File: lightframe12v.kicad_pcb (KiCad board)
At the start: 2 copper layers, 91.4 x 45.7 mm, 44 parts, among them J1 PJ-077, J2 Conn_01x06_Female, J3 Conn_01x02_Female, J4 Conn_01x06_Female, J5 Conn_01x04_Female, J6 Conn_01x6_Female, Q1 MMBT2222A-TP, Q2 MMBT2222A-TP, SW1 SW_Push, SW2 SW_Push, U1 TPS562211, U2 ESP32-WROOM-32U, U3 TLC5971

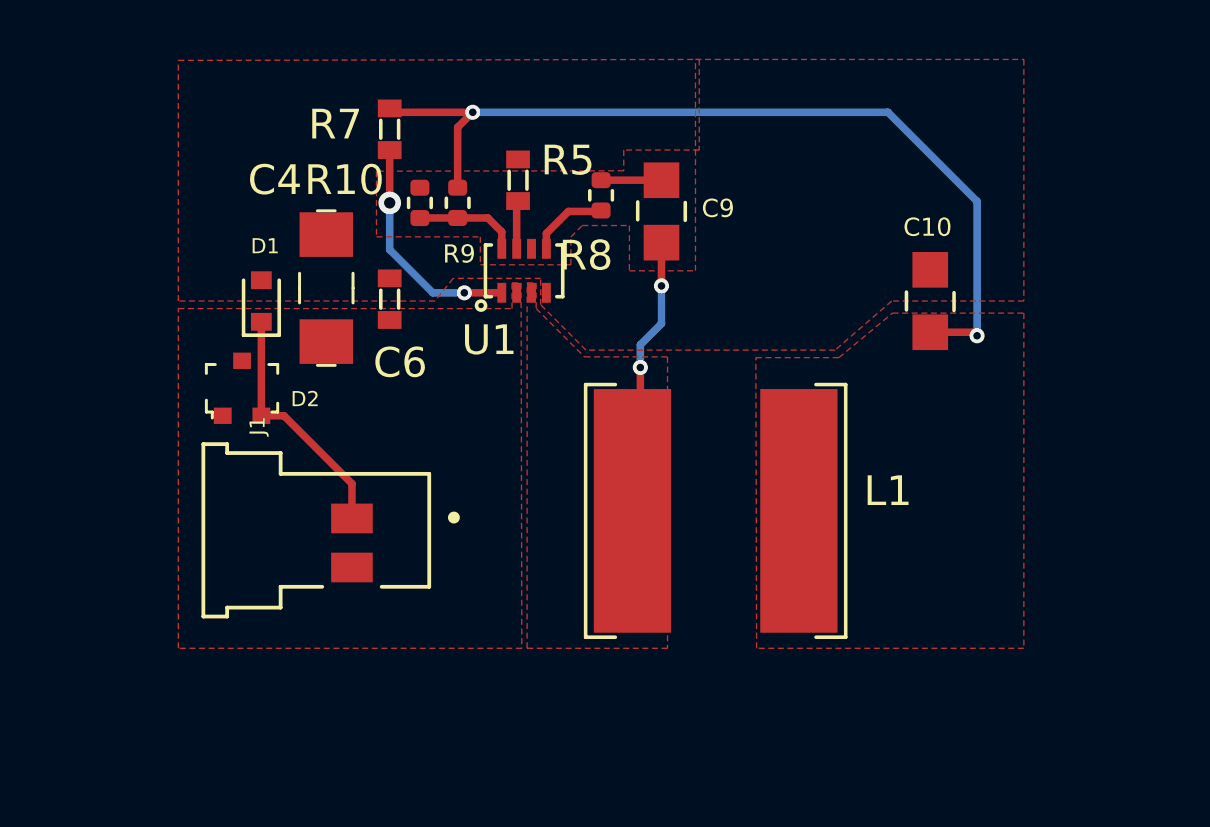
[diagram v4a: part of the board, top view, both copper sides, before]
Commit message: Top ground no cutouts.
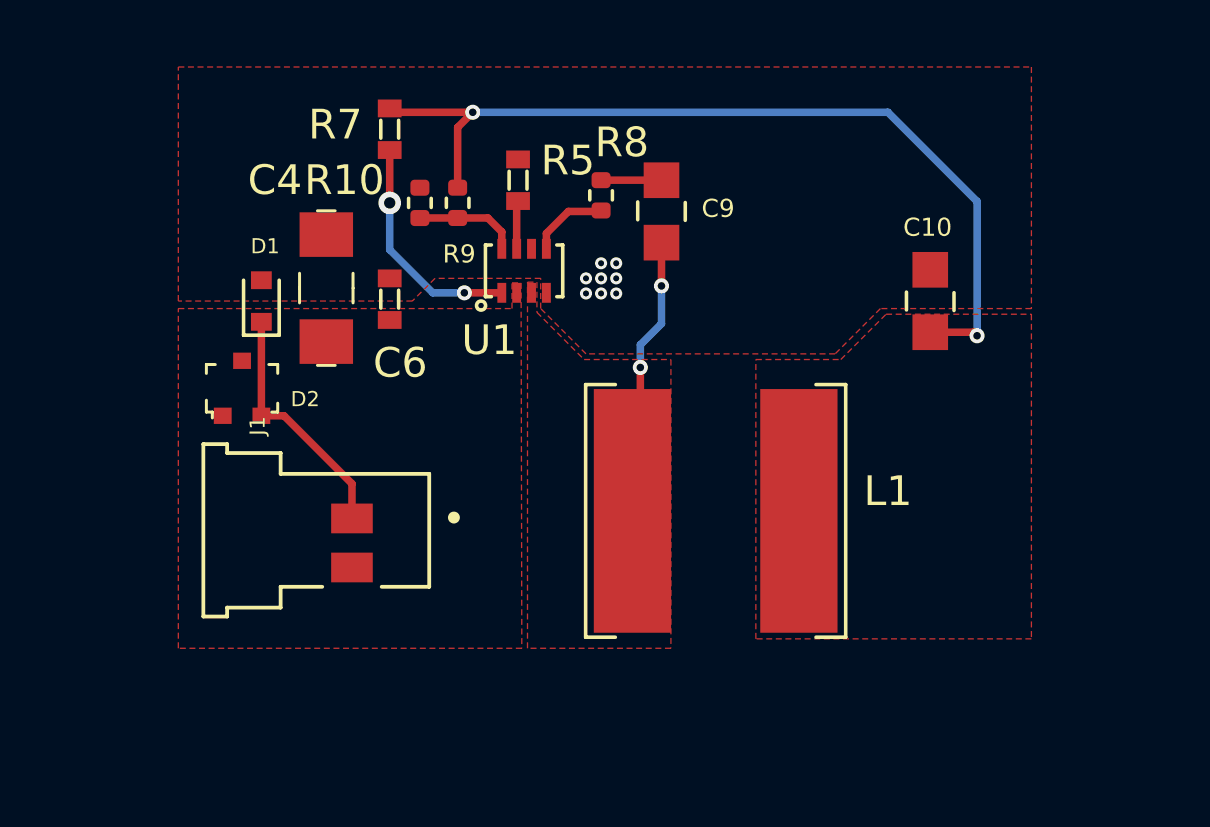
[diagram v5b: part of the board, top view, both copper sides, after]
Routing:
- net GND: vias 18 -> 26
- removed copper zone on F.Cu, net +3V3
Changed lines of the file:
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@@
     (thickness 1.6)
     (drawings 4)
-    (tracks 339)
+    (tracks 347)
     (zones 0)
     (modules 44)
@@
     (tags resistor)
     (attr smd)
-    (fp_text reference R8 (at -2.032 -0.508 180) (layer F.SilkS)
+    (fp_text reference R8 (at 1.778 0.6985 180) (layer F.SilkS)
       (effects (font (size 1 1) (thickness 0.15)))
     )
@@
   (segment (start 280.67 -530.352) (end 280.67 -530.352) (width 0.254) (layer F.Cu) (net 1))
   (via (at 280.67 -530.352) (size 0.508) (drill 0.254) (layers F.Cu B.Cu) (net 1))
+  (via (at 345.44 -560.324) (size 0.4064) (drill 0.2032) (layers F.Cu B.Cu) (net 1))
+  (via (at 345.44 -559.816) (size 0.4064) (drill 0.2032) (layers F.Cu B.Cu) (net 1))
+  (via (at 345.948 -559.816) (size 0.4064) (drill 0.2032) (layers F.Cu B.Cu) (net 1))
+  (via (at 345.948 -560.324) (size 0.4064) (drill 0.2032) (layers F.Cu B.Cu) (net 1))
+  (via (at 346.456 -560.324) (size 0.4064) (drill 0.2032) (layers F.Cu B.Cu) (net 1))
+  (via (at 346.456 -559.816) (size 0.4064) (drill 0.2032) (layers F.Cu B.Cu) (net 1))
+  (via (at 345.948 -560.832) (size 0.4064) (drill 0.2032) (layers F.Cu B.Cu) (net 1))
+  (via (at 346.456 -560.832) (size 0.4064) (drill 0.2032) (layers F.Cu B.Cu) (net 1))
   (segment (start 321.564 -530.606) (end 313.436 -530.606) (width 0.508) (layer F.Cu) (net 2))
   (segment (start 311.402 -532.64) (end 313.436 -530.606) (width 0.508) (layer F.Cu) (net 2))
@@
     )
   )
-  (zone (net 38) (net_name "Net-(C9-Pad2)") (layer F.Cu) (hatch edge 0.508)
+  (zone (net 1) (net_name GND) (layer F.Cu) (hatch full 0.508)
     (connect_pads (clearance 0.1524))
     (min_thickness 0.254)
@@
     (polygon
       (pts
-        (xy 343.7636 -559.308) (xy 345.3892 -557.6824) (xy 348.1832 -557.6824) (xy 348.1832 -547.878) (xy 343.4588 -547.878)
-        (xy 343.4588 -560.1716) (xy 343.7636 -560.1716)
+        (xy 360.426 -559.308) (xy 355.346 -559.308) (xy 353.822 -557.784) (xy 345.44 -557.784) (xy 343.916 -559.308)
+        (xy 343.916 -560.324) (xy 340.36 -560.324) (xy 339.598 -559.562) (xy 331.724 -559.562) (xy 331.724 -567.436)
+        (xy 360.426 -567.436)
       )
     )
   )
-  (zone (net 2) (net_name +3V3) (layer F.Cu) (hatch edge 0.508)
+  (zone (net 38) (net_name "Net-(C9-Pad2)") (layer F.Cu) (hatch full 0.508)
     (connect_pads (clearance 0.1524))
     (min_thickness 0.254)
@@
     (polygon
       (pts
-        (xy 360.172 -547.878) (xy 351.1804 -547.878) (xy 351.155 -557.657) (xy 353.949 -557.657) (xy 355.7524 -559.1556)
-        (xy 360.172 -559.1556)
+        (xy 343.789 -559.181) (xy 345.3765 -557.5935) (xy 348.2975 -557.5935) (xy 348.2975 -547.878) (xy 343.4715 -547.878)
+        (xy 343.4715 -560.197) (xy 343.789 -560.197)
       )
     )
   )
-  (zone (net 1) (net_name GND) (layer F.Cu) (hatch edge 0.508)
+  (zone (net 38) (net_name "Net-(C9-Pad2)") (layer F.Cu) (hatch full 0.508)
     (connect_pads (clearance 0.1524))
     (min_thickness 0.254)
@@
     (polygon
       (pts
-        (xy 349.25 -567.69) (xy 349.25 -564.642) (xy 346.71 -564.642) (xy 346.71 -563.9435) (xy 338.3915 -563.930863)
-        (xy 338.3915 -561.721) (xy 341.884 -561.721) (xy 341.884 -560.7812) (xy 344.932 -560.7812) (xy 344.932 -561.721)
-        (xy 345.313 -562.102) (xy 346.9005 -562.102) (xy 346.9005 -560.578) (xy 349.123 -560.578) (xy 349.123 -567.69)
-        (xy 360.172 -567.69) (xy 360.172 -559.562) (xy 355.727 -559.562) (xy 353.822 -557.911) (xy 345.44 -557.911)
-        (xy 343.916 -559.435) (xy 343.916 -560.324) (xy 340.9696 -560.324) (xy 340.36 -559.562) (xy 331.724 -559.562)
-        (xy 331.724 -567.65825)
+        (xy 360.426 -548.1955) (xy 351.155 -548.1955) (xy 351.155 -557.5935) (xy 354.0125 -557.5935) (xy 355.5365 -559.1175)
+        (xy 360.426 -559.1175)
       )
     )

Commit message: Pmic refactor.
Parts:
- added TP1: wall in, TestPoint:TestPoint_Pad_1.5x1.5mm, F.Cu at (340.9, -550.0)
- added TP3: pgss, TestPoint:TestPoint_Pad_1.5x1.5mm, F.Cu at (332.5, -563.4)
- added TP4: 3v3 out, TestPoint:TestPoint_Pad_1.5x1.5mm, F.Cu at (358.0, -548.6)
- R10, R8, R9: footprint Resistor_SMD:R_0402_1005Metric -> digikey-footprints:0603
- moved R7 3.42 mm to (335.7, -564.1)
- moved J1 2.79 mm to (334.1, -550.0)
- moved C4 2.28 mm to (337.6, -557.9)
- moved C10 2.03 mm to (355.8, -557.9)
- moved D2 1.89 mm to (332.6, -555.2)
- moved R10 1.79 mm to (338.1, -562.7)
- moved C6 1.71 mm to (340.1, -558.5)
- moved D1 1.48 mm to (333.9, -558.2)
- moved U1 1.40 mm to (343.4, -559.2)
- moved L1 1.07 mm to (349.8, -551.4)
- moved R5 0.96 mm to (343.0, -562.7)
- moved C9 0.72 mm to (348.5, -562.1)
- moved R9 0.66 mm to (340.5, -562.7)
- moved R8 0.46 mm to (345.8, -562.7)
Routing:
- net Net-(R7-Pad2): track 7.73 -> 14.6 mm
- net Net-(R10-Pad1): track 3.52 -> 5.87 mm
- net +3V3: track 86.0 -> 88.1 mm
- net GND: track 26.8 -> 28.8 mm, vias 26 -> 88
- net Net-(C9-Pad2): track 9.43 -> 10.6 mm
- net Net-(C9-Pad1): track 2.03 -> 2.77 mm
- net Net-(R8-Pad1): track 2.61 -> 3.21 mm
- net (no net): vias 0 -> 2
- added copper zone on B.Cu, net +12V
- added copper zone on F.Cu, net +3V3
- removed copper zone on B.Cu, net GND

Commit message: More layout.
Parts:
- removed J3: Conn_01x02_Female, Connector_PinSocket_2.54mm:PinSocket_1x02_P2.54mm_Vertical
- added TP2: ground test, TestPoint:TestPoint_Pad_1.5x1.5mm, F.Cu at (353.8, -511.8)
- J2, J4: value Conn_01x06_Female -> Conn_01x07_Female; footprint Connector_PinSocket_2.54mm:PinSocket_1x06_P2.54mm_Vertical -> Connector_PinHeader_2.54mm:PinHeader_1x07_P2.54mm_Vertical
- J6: value Conn_01x6_Female -> Conn_01x4_Female; footprint Connector_PinSocket_2.54mm:PinSocket_1x06_P2.54mm_Vertical -> Connector_PinHeader_2.54mm:PinHeader_1x04_P2.54mm_Vertical
- moved J2 86.9 mm to (361.2, -536.4), turned to 270 degrees
- moved J4 65.4 mm to (337.1, -536.4), turned to 270 degrees
- moved TP3 58.5 mm to (352.3, -508.3), turned to 180 degrees
- moved R7 58.2 mm to (349.8, -507.6), turned to 90 degrees
- moved R11 58.2 mm to (341.1, -526.0)
- moved R10 54.5 mm to (347.4, -509.0), turned to 270 degrees
- moved R8 54.0 mm to (339.6, -509.0), turned to 270 degrees
- moved R9 53.9 mm to (345.0, -509.0), turned to 90 degrees
- moved C9 53.7 mm to (337.0, -509.6), turned to 90 degrees
- moved R5 53.7 mm to (342.4, -509.0), turned to 90 degrees
- moved U3 53.1 mm to (338.3, -530.5), turned to 180 degrees
- moved C10 51.3 mm to (329.7, -513.7), turned to 270 degrees
- moved C11 49.1 mm to (336.2, -526.0), turned to 0 degrees
- moved D1 48.2 mm to (351.6, -513.4), turned to 270 degrees
- moved U1 46.7 mm to (342.1, -512.5), turned to 270 degrees
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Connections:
- J6 pad 3: /Gpio33 -> /Gpio35
- J6 pad 4: /Gpio32 -> /Gpio34
- Q2 pad 2: /Gpio0 -> /Dtr
- Q2 pad 3: /Dtr -> /Gpio0
- U2 pad 26: /Serial_Clock -> Net-(U2-Pad26)
- U2 pad 27: /Serial_In -> Net-(U2-Pad27)
- U2 pad 8: /Gpio32 -> /Serial_In
- U2 pad 9: /Gpio33 -> /Serial_Clock
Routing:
- net /LED12: track 37.2 -> 0.00 mm
- net /LED11: track 33.4 -> 0.00 mm
- net /LED10: track 29.7 -> 0.00 mm
- net +3V3: track 88.1 -> 60.6 mm
- net /LED9: track 26.4 -> 0.00 mm
- net /LED8: track 23.3 -> 0.00 mm
- net /Serial_Clock: track 25.7 -> 45.8 mm
- net /LED7: track 20.5 -> 0.79 mm
- net /Serial_In: track 32.0 -> 47.5 mm
- net /LED1: track 12.3 -> 0.16 mm
- net /Gpio27: track 10.1 -> 0.00 mm, vias 2 -> 0
- net /LED2: track 9.93 -> 0.00 mm
- net /LED6: track 10.2 -> 0.45 mm
- net /Gpio33: track 9.51 -> 0.00 mm, vias 2 -> 0
- net /LED3: track 9.15 -> 0.00 mm
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
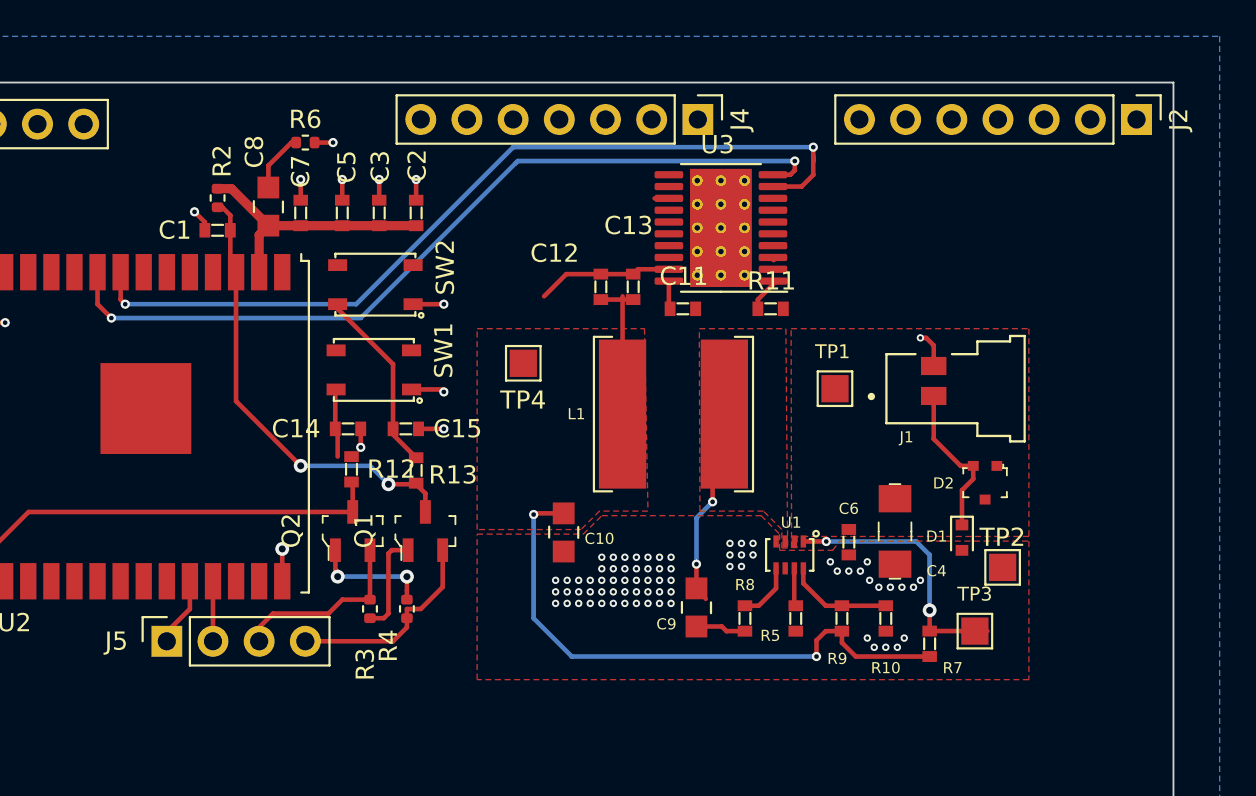
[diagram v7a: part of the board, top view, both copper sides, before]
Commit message: Plane cleanup and power rails.
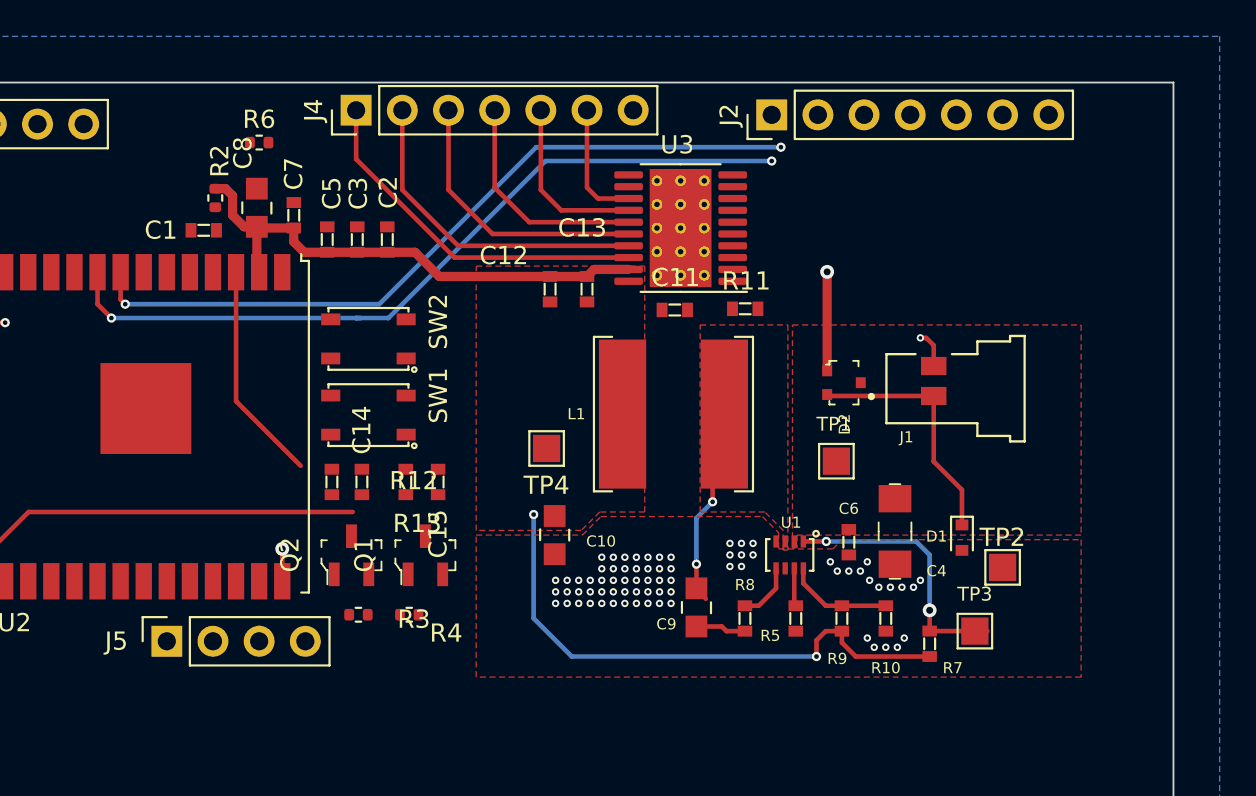
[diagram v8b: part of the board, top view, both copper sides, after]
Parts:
- moved J2 20.1 mm to (341.1, -536.7), turned to 90 degrees
- moved J4 18.8 mm to (318.3, -537.0), turned to 90 degrees
- moved D2 9.51 mm to (345.1, -522.0), turned to 0 degrees
- moved TP4 4.86 mm to (328.7, -518.4)
- moved TP1 3.99 mm to (344.7, -517.7)
- moved C15 3.42 mm to (322.8, -516.5), turned to 90 degrees
- moved C14 3.02 mm to (318.6, -516.5), turned to 90 degrees
- moved SW2 3.01 mm to (318.9, -524.4)
- moved C12 2.80 mm to (328.9, -527.1)
- moved C13 2.54 mm to (331.0, -527.1)
- moved R6 2.54 mm to (312.9, -535.2)
- moved SW1 2.50 mm to (318.9, -520.2)
- moved U3 2.22 mm to (336.1, -530.5)
- moved C2 2.16 mm to (320.0, -529.8)
- moved C3 1.90 mm to (318.3, -529.8)
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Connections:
- J2 pad 1: /LED1 -> /LED6
- J2 pad 2: /LED2 -> /LED5
- J2 pad 3: /LED3 -> /LED4
- J2 pad 4: /LED4 -> /LED3
- J2 pad 5: /LED5 -> /LED2
- J2 pad 6: /LED6 -> /LED1
- J4 pad 1: /LED7 -> /LED12
- J4 pad 2: /LED8 -> /LED11
- J4 pad 3: /LED9 -> /LED10
- J4 pad 4: /LED10 -> /LED9
- J4 pad 5: /LED11 -> /LED8
- J4 pad 6: /LED12 -> /LED7
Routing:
- net /LED12: track 0.00 -> 19.9 mm
- net /LED11: track 0.00 -> 18.1 mm
- net /LED10: track 0.00 -> 15.3 mm
- net GND: track 20.6 -> 6.10 mm, vias 82 -> 72
- net /LED9: track 0.00 -> 12.4 mm
- net /Reset: track 24.9 -> 12.6 mm, vias 2 -> 0
- net /Rts: track 11.4 -> 0.00 mm
- net Net-(C15-Pad2): track 10.2 -> 0.00 mm
- net /LED8: track 0.00 -> 9.67 mm
- net /Dtr: track 10.2 -> 0.76 mm
- net Net-(Q2-Pad1): track 6.58 -> 0.00 mm, vias 2 -> 0
- net /Serial_In: track 47.5 -> 41.5 mm
- net /LED7: track 0.79 -> 6.79 mm
- net Net-(Q1-Pad1): track 5.58 -> 0.00 mm
- net +12V: track 0.00 -> 5.57 mm, vias 0 -> 1
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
